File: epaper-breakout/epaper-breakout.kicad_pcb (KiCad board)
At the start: 2 copper layers, 100 x 45 mm, 102 parts, among them J1 XF2M-3315-1A, J2 C10418, J3 Conn_02x05_Counter_Clockwise, J4 ED060SC4, J5 Conn_01x01_Male, J6 Conn_01x01_Male, J7 Conn_01x12, Q3 MMBT3904, Q4 MMBT3904, U1 MCP1700-3302E_SOT23, U11 TP4056, U12 CH340C, U2 PCA9555PW, U3 TPS651851RSLR, U4 XC6206PxxxMR, U5 ESP32-WROVER, U6 ED060XC5, U7 TPS2113APW

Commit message: new v6 routing
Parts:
- removed J6: Conn_01x01_Male, Connector_PinHeader_2.54mm:PinHeader_1x01_P2.54mm_Vertical
- removed the REF** at (120.7, 24.1)
- removed TP_VCOM1: VCOM, TestPoint:TestPoint_Pad_D2.0mm
- added C40: 0.1uF, Capacitor_SMD:C_0805_2012Metric, F.Cu at (65.6, 22.0)
- added CC: Symbol_CreativeCommons_SilkScreenTop_Type2_Big, Symbol:Symbol_CreativeCommons_SilkScreenTop_Type2_Big, B.Cu at (117.2, 56.8)
- added REF**: OSHW-Logo2_7.3x6mm_Copper, Symbol:OSHW-Logo2_7.3x6mm_Copper, F.Cu at (115.5, 23.5)
- added TP1: +22V, TestPoint:TestPoint_Pad_D2.5mm, F.Cu at (48.0, 60.5)
- added TP2: +15V, TestPoint:TestPoint_Pad_D2.5mm, F.Cu at (52.0, 60.5)
- added TP3: -20V, TestPoint:TestPoint_Pad_D2.5mm, F.Cu at (44.0, 60.5)
- added TP4: -15V, TestPoint:TestPoint_Pad_D2.5mm, F.Cu at (56.0, 60.5)
- added TP5: VCOM, TestPoint:TestPoint_Pad_D2.5mm, F.Cu at (70.0, 60.5)
- J5: value Conn_01x01_Male -> Conn_01x02_Female; footprint Connector_PinHeader_2.54mm:PinHeader_1x01_P2.54mm_Vertical -> Connector_PinHeader_2.54mm:PinHeader_1x02_P2.54mm_Vertical
- moved C23 51.9 mm to (29.2, 50.2), turned to 0 degrees
- moved JP_BAT1 40.4 mm to (41.0, 45.0)
- moved R26 36.3 mm to (121.6, 58.3), turned to 0 degrees
- moved C34 34.2 mm to (121.6, 56.3), turned to 0 degrees
- moved R15 33.6 mm to (77.2, 31.2), turned to 0 degrees
- moved R28 32.1 mm to (121.5, 54.2), turned to 0 degrees
- moved C36 30.3 mm to (121.6, 52.2), turned to 0 degrees
- moved C19 28.8 mm to (121.8, 50.0), turned to 0 degrees
- moved H2 24.5 mm to (27.5, 62.0)
- moved C35 19.8 mm to (113.9, 45.6)
- moved C37 19.7 mm to (114.0, 49.4)
- moved R27 19.7 mm to (113.8, 47.5)
- moved R29 19.6 mm to (113.8, 51.4)
- moved C39 19.2 mm to (41.0, 41.6), turned to 0 degrees
- moved C38 18.7 mm to (114.0, 53.5)
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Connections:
- net Net-(J2-Pad2) renamed /USB_D-
- net Net-(J2-Pad3) renamed /USB_D+
- J1 pad 2: (no net) -> Net-(J1-Pad2)
- J1 pad 21: (no net) -> Net-(J1-Pad21)
- J1 pad 23: (no net) -> Net-(J1-Pad23)
- J1 pad 25: (no net) -> Net-(J1-Pad25)
- J1 pad 27: (no net) -> Net-(J1-Pad27)
- J1 pad 34: (no net) -> Net-(J1-Pad34)
- J1 pad 35: (no net) -> Net-(J1-Pad35)
- J1 pad 4: (no net) -> Net-(J1-Pad4)
- J1 pad 6: (no net) -> Net-(J1-Pad6)
- J2 pad 4: (no net) -> Net-(J2-Pad4)
- J4 pad 20: (no net) -> Net-(J4-Pad20)
- J4 pad 21: (no net) -> Net-(J4-Pad21)
- J4 pad 25: (no net) -> Net-(J4-Pad25)
- J4 pad 26: (no net) -> Net-(J4-Pad26)
- J4 pad 39: (no net) -> Net-(J4-Pad39)
- J5 pad 1: BAT+ -> GND
- U11 pad 9: (no net) -> Net-(U11-Pad9)
- U12 pad 10: (no net) -> Net-(U12-Pad10)
- U12 pad 11: (no net) -> Net-(U12-Pad11)
- U12 pad 12: (no net) -> Net-(U12-Pad12)
- U12 pad 15: (no net) -> Net-(U12-Pad15)
- U12 pad 7: (no net) -> Net-(U12-Pad7)
- U12 pad 8: (no net) -> Net-(U12-Pad8)
- U12 pad 9: (no net) -> Net-(U12-Pad9)
- U3 pad 11: (no net) -> Net-(U3-Pad11)
- U3 pad 13: (no net) -> Net-(U3-Pad13)
- U3 pad 20: (no net) -> Net-(U3-Pad20)
- U3 pad 38: (no net) -> Net-(U3-Pad38)
- U3 pad 39: (no net) -> Net-(U3-Pad39)
- U5 pad 17: (no net) -> Net-(U5-Pad17)
- U5 pad 18: (no net) -> Net-(U5-Pad18)
- U5 pad 19: (no net) -> Net-(U5-Pad19)
- U5 pad 20: (no net) -> Net-(U5-Pad20)
- U5 pad 21: (no net) -> Net-(U5-Pad21)
- U5 pad 22: (no net) -> Net-(U5-Pad22)
- U5 pad 27: (no net) -> Net-(U5-Pad27)
- U5 pad 28: (no net) -> Net-(U5-Pad28)
- U5 pad 32: (no net) -> Net-(U5-Pad32)
- U6 pad 22: (no net) -> Net-(U6-Pad22)
- U6 pad 23: (no net) -> Net-(U6-Pad23)
- U6 pad 24: (no net) -> Net-(U6-Pad24)
- U6 pad 25: (no net) -> Net-(U6-Pad25)
- U6 pad 30: (no net) -> Net-(U6-Pad30)
- U6 pad 4: (no net) -> Net-(U6-Pad4)
- U6 pad 5: (no net) -> Net-(U6-Pad5)
- U7 pad 1: (no net) -> Net-(U7-Pad1)
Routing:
- net EPD_VDD: track 155.2 -> 38.9 mm, vias 10 -> 13
- net GND: track 186.6 -> 294.3 mm, vias 259 -> 129
- net /+3.3V: track 165.3 -> 85.8 mm, vias 11 -> 13
- net Net-(C23-Pad2): track 61.8 -> 13.6 mm, vias 2 -> 0
- net /A0: track 47.9 -> 94.4 mm
- net /+22V: track 169.3 -> 141.4 mm, vias 7 -> 5
- net /VNEG_IN: track 35.9 -> 63.3 mm, vias 0 -> 4
- net SW_VIN: track 114.0 -> 89.9 mm, vias 5 -> 21
- net /SCL: track 63.1 -> 83.4 mm, vias 3 -> 6
- net /-20V: track 144.9 -> 164.7 mm, vias 5 -> 9
- net /-15V: track 109.6 -> 129.3 mm, vias 7 -> 2
- net /EP_STV: track 126.6 -> 144.7 mm
- net /EP_LE: track 55.5 -> 72.4 mm
- net /~RTS: track 23.5 -> 6.55 mm
- net Net-(C26-Pad2): track 17.8 -> 34.2 mm, vias 2 -> 0
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- added copper zone on In2.Cu, net /+3.3V
- added copper zone on B.Cu, net /VNEG_IN
- added copper zone on In2.Cu, net EPD_VDD
- added copper zone on In1.Cu, net GND
- added copper zone on F.Cu, net SW_VIN
- added copper zone on In2.Cu, net SW_VIN
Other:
- outline, holes or cut-outs redrawn
- copper layers 2 -> 4
- board text added: "epdiy v6 by Valentin Roland 2021 Thanks to the epdiy contributors! For sources and documentation visit https://github.com/vroland/epdiy"
- board text removed: "epdiy v6 by Valentin Roland 2021 Thanks to the epdiy contributors!"

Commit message: manufacturing files
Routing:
- net GND: vias 129 -> 134
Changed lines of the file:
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@@
     (thickness 1.6)
     (drawings 56)
-    (tracks 2379)
+    (tracks 2384)
     (zones 0)
     (modules 107)
@@
     (visible_elements 7FFFFFFF)
     (pcbplotparams
-      (layerselection 0x010fc_ffffffff)
+      (layerselection 0x310fc_ffffffff)
       (usegerberextensions true)
-      (usegerberattributes false)
+      (usegerberattributes true)
       (usegerberadvancedattributes false)
       (creategerberjobfile false)
@@
       (psa4output false)
       (plotreference true)
-      (plotvalue false)
+      (plotvalue true)
       (plotinvisibletext false)
       (padsonsilk false)
@@
   (segment (start 109.5 28.699198) (end 108.449198 29.75) (width 0.3) (layer In1.Cu) (net 1))
   (segment (start 109.5 27.75) (end 109.5 28.699198) (width 0.3) (layer In1.Cu) (net 1))
+  (via (at 90 35.5) (size 0.8) (drill 0.4) (layers F.Cu B.Cu) (net 1))
+  (via (at 90 33.75) (size 0.8) (drill 0.4) (layers F.Cu B.Cu) (net 1))
+  (via (at 102.5 35.25) (size 0.8) (drill 0.4) (layers F.Cu B.Cu) (net 1))
+  (via (at 102.5 31.5) (size 0.8) (drill 0.4) (layers F.Cu B.Cu) (net 1))
+  (via (at 102.5 32.75) (size 0.8) (drill 0.4) (layers F.Cu B.Cu) (net 1))
   (segment (start 72.6973 45.212) (end 72.71 45.2247) (width 0.5) (layer F.Cu) (net 2))
   (segment (start 67.999 46.028) (end 69.161 46.028) (width 0.2) (layer F.Cu) (net 2))

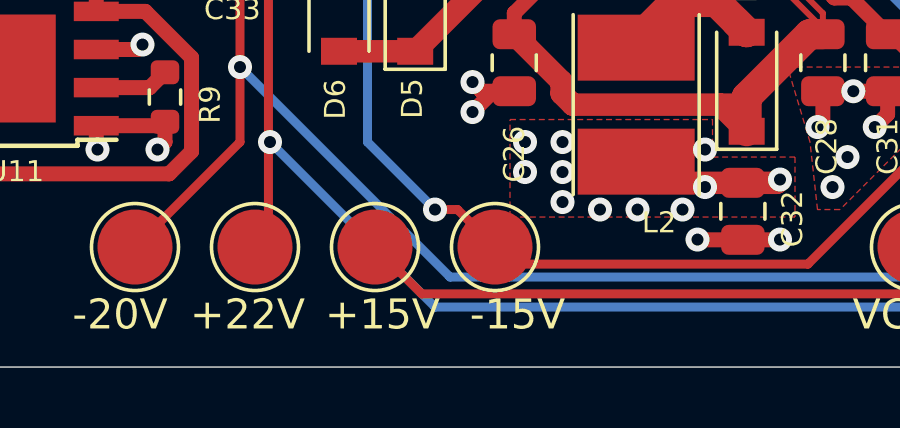
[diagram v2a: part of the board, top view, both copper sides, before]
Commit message: fix testpoint labels
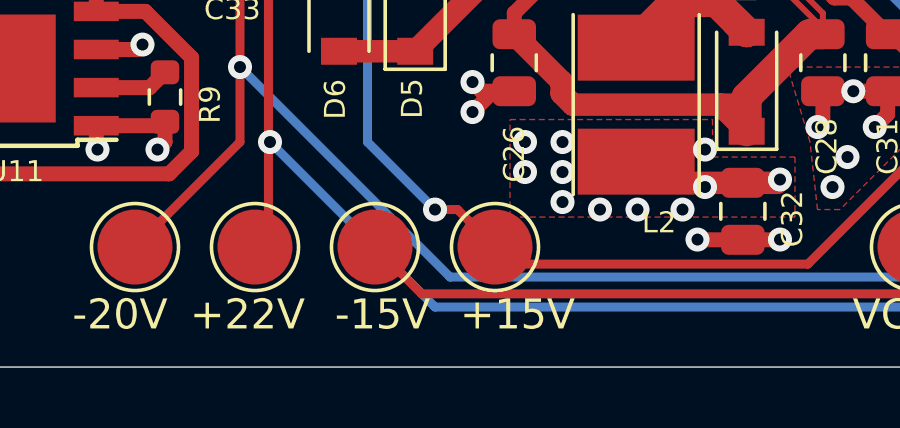
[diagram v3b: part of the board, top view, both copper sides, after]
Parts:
- TP2: value +15V -> -15V
- TP4: value -15V -> +15V

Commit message: updated manufacturing files
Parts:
- removed the REF** at (115.5, 23.5)
- added REF**: oshw_surface, epaper-breakout:oshw_surface, F.Cu at (115.5, 23.5)

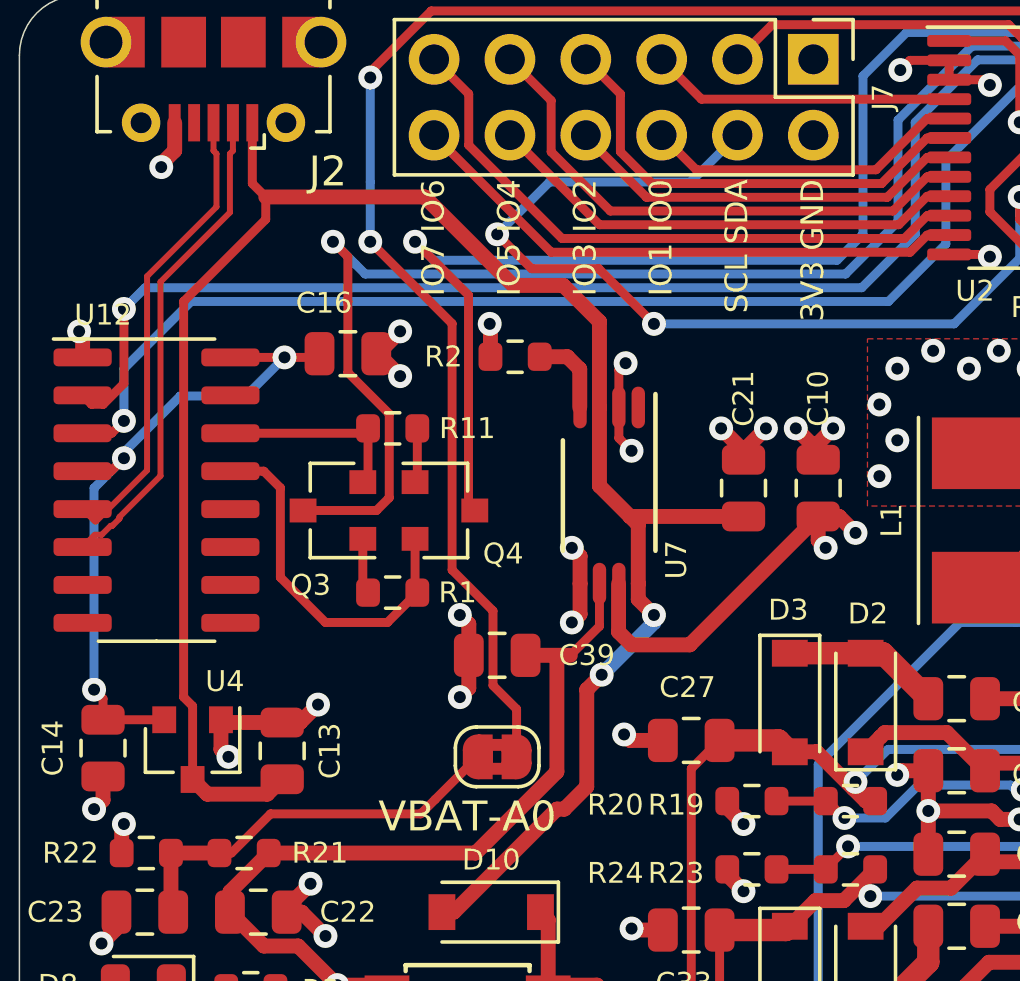
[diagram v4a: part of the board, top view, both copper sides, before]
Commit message: v6: fix battery switchover
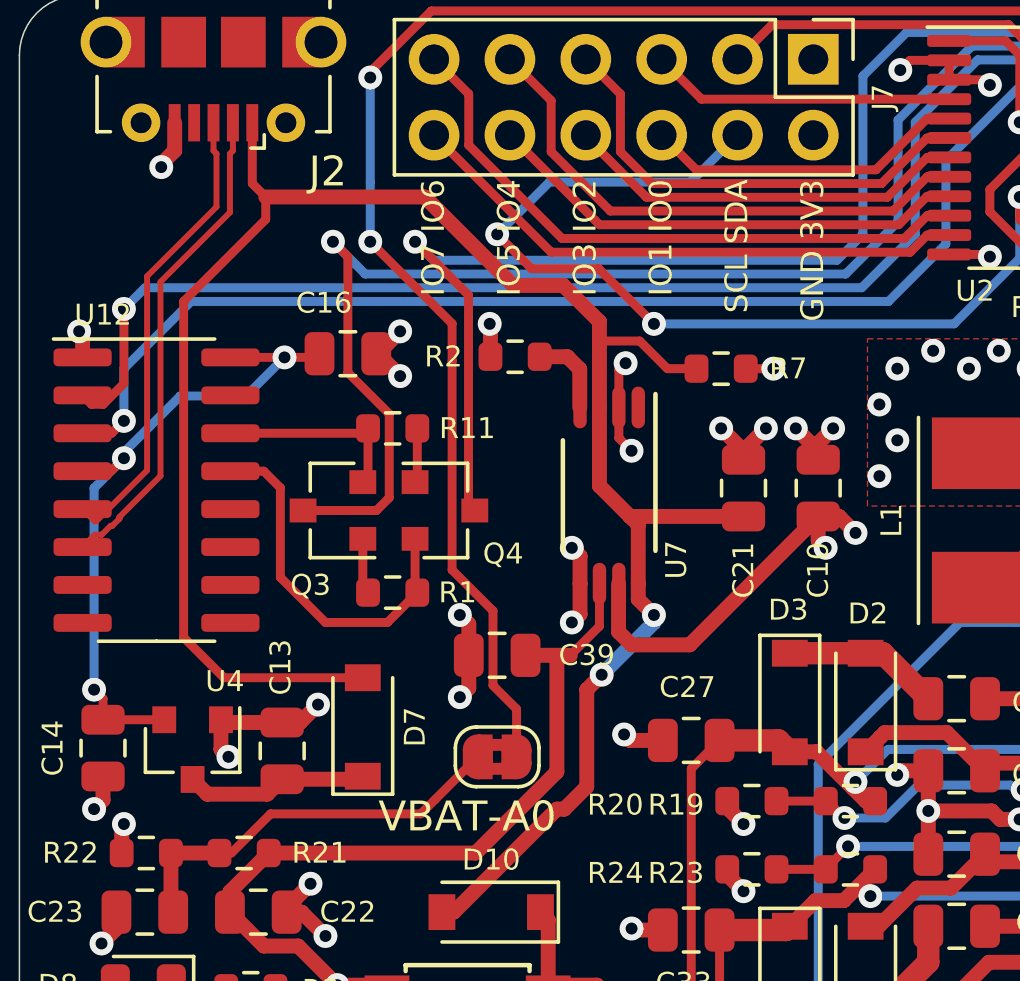
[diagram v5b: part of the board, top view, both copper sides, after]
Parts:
- added D7: 1N5817, Diode_SMD:D_SOD-123, F.Cu at (36.5, 44.0)
- added R7: 100k, Resistor_SMD:R_0603_1608Metric, F.Cu at (48.5, 32.0)
- U2: value PCA9555PW -> PCA9535PW
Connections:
- C13 pad 1: VBUS -> Net-(C13-Pad1)
- U4 pad 3: VBUS -> Net-(C13-Pad1)
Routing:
- net Net-(C13-Pad1): track 0.00 -> 6.15 mm
- net VBUS: track 67.4 -> 69.3 mm
- net GND: track 294.3 -> 295.2 mm, vias 134 -> 135
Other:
- board text added: "GND 3V3"
